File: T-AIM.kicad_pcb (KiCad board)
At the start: 2 copper layers, 3 parts, among them IC1 ATMEGA328PB-A, U1 V7805-500-SMT, U2 78L05

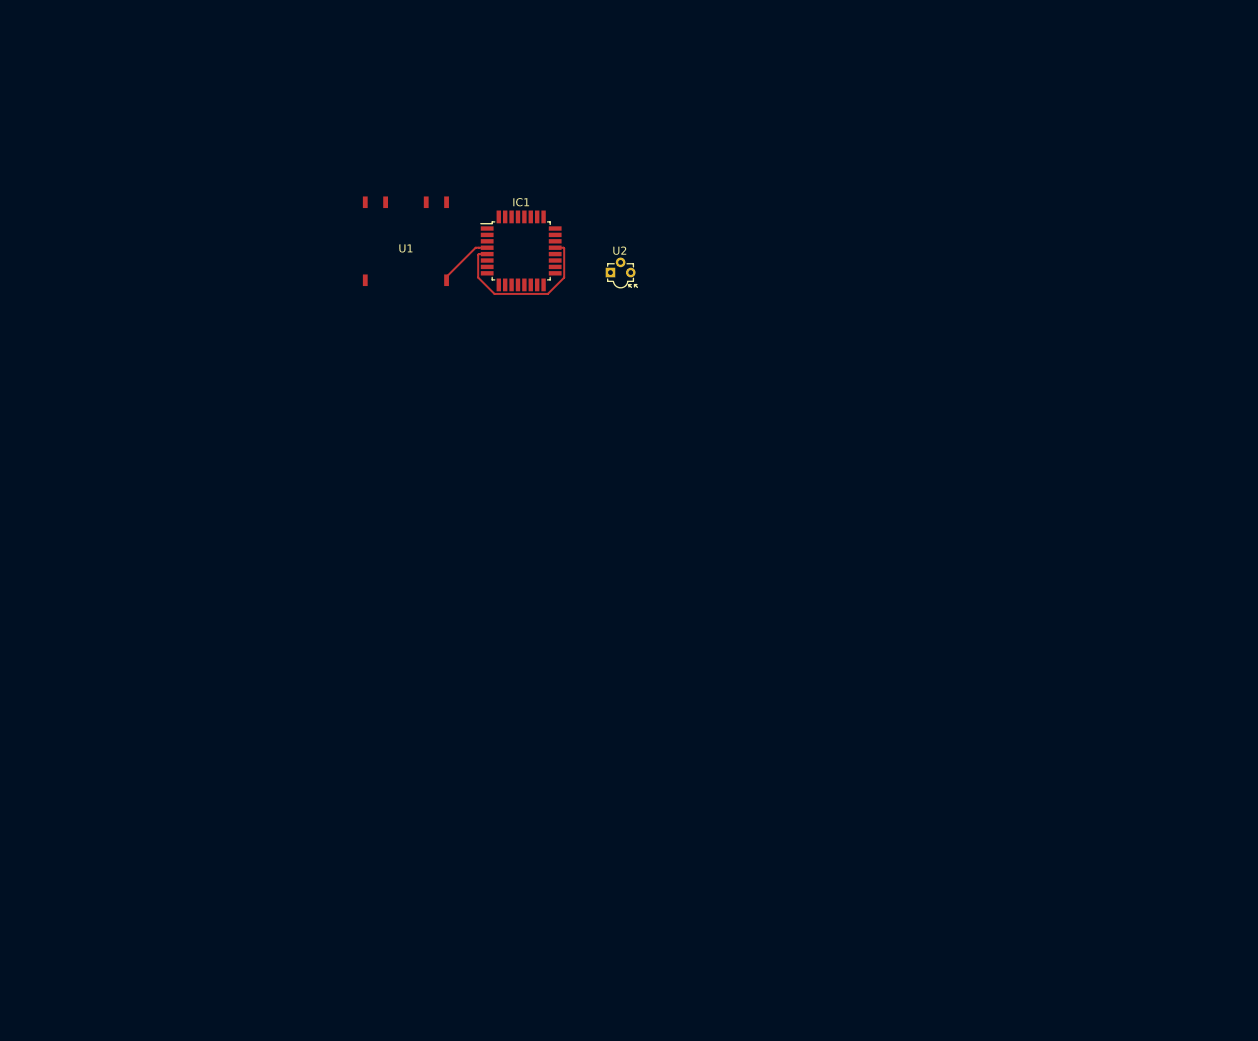
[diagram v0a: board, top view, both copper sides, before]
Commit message: Schematic switches changed; PCB footprints assigned; Preliminary PCB layout set
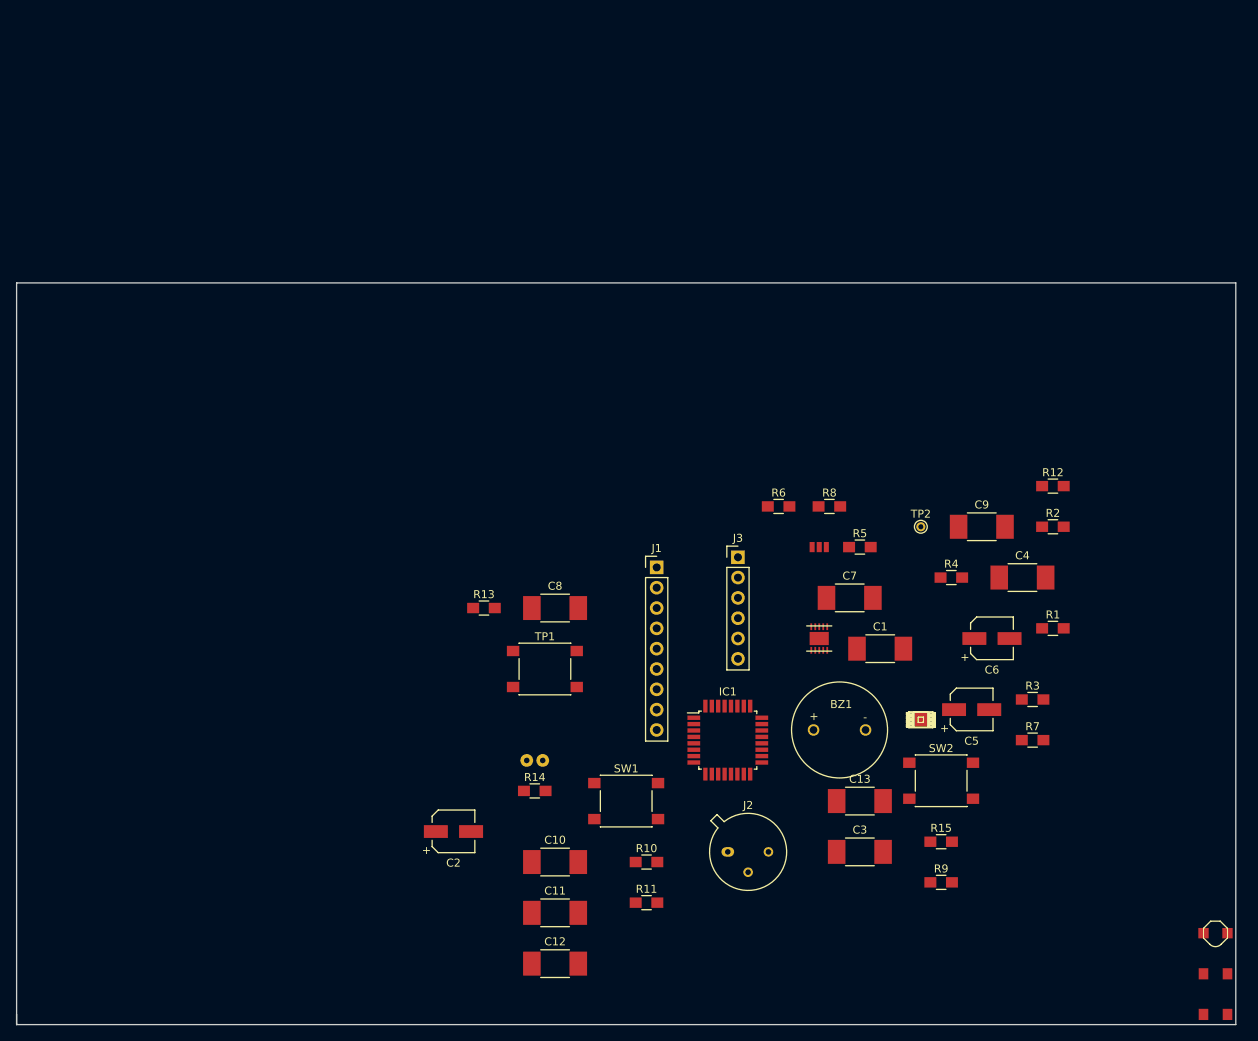
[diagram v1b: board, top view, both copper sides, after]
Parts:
- removed U2: 78L05, Opto-Devices:OPIC_Sharp_IS485
- added BZ1: Alarm Buzzer, T-AIM:AT-1220-TT-9-R, F.Cu at (167.6, 106.7)
- added C1: 10uF, Capacitors_SMD:C_1812_HandSoldering, F.Cu at (172.7, 96.5)
- added C10: 22uF, Capacitors_SMD:C_1812_HandSoldering, F.Cu at (132.1, 123.2)
- added C11: 0.1uF, Capacitors_SMD:C_1812_HandSoldering, F.Cu at (132.1, 129.5)
- added C12: 0.1uF, Capacitors_SMD:C_1812_HandSoldering, F.Cu at (132.1, 135.9)
- added C13: 0.1uF, Capacitors_SMD:C_1812_HandSoldering, F.Cu at (170.2, 115.6)
- added C2: 10uF, Capacitors_SMD:CP_Elec_5x5.3, F.Cu at (119.4, 119.4)
- added C3: 0.1uF, Capacitors_SMD:C_1812_HandSoldering, F.Cu at (170.2, 121.9)
- added C4: 0.1uF, Capacitors_SMD:C_1812_HandSoldering, F.Cu at (190.5, 87.6)
- added C5: 1uF, Capacitors_SMD:CP_Elec_5x5.3, F.Cu at (184.2, 104.1)
- added C6: 10nF, Capacitors_SMD:CP_Elec_5x5.3, F.Cu at (186.7, 95.2)
- added C7: 0.1uF, Capacitors_SMD:C_1812_HandSoldering, F.Cu at (168.9, 90.2)
- added C8: 22pF, Capacitors_SMD:C_1812_HandSoldering, F.Cu at (132.1, 91.4)
- added C9: 22pF, Capacitors_SMD:C_1812_HandSoldering, F.Cu at (185.4, 81.3)
- added D1: Red LED, SparkFun-LED:LED-1206, F.Cu at (214.6, 137.2)
- added D2: Blue LED, SparkFun-LED:LED-1206, F.Cu at (214.6, 142.2)
- added IC2: MAX17043, SparkFun-PowerIC:TDFN-8, F.Cu at (177.8, 105.4)
- added J1: ADXL345 Connector, Pin_Headers:Pin_Header_Straight_1x09_Pitch2.54mm, F.Cu at (144.8, 86.4)
- added J2: PIR Sensor Connector, TO_SOT_Packages_THT:TO-5-3, F.Cu at (153.7, 121.9)
- added J3: JY-MCU HC-05 Pins, Pin_Headers:Pin_Header_Straight_1x06_Pitch2.54mm, F.Cu at (154.9, 85.1)
- added JP1: M02JST-PTH-2, SparkFun-Connectors:JST-2-PTH, F.Cu at (129.5, 110.5)
- added L1: 4.7uH, 1.2A, SparkFun-Passives:INDUCTOR_4.7UH, F.Cu at (214.6, 132.1)
- added R1: 2M, Resistors_SMD:R_0805_HandSoldering, F.Cu at (194.3, 94.0)
- added R10: 10k, Resistors_SMD:R_0805_HandSoldering, F.Cu at (143.5, 123.2)
- added R11: 1k, Resistors_SMD:R_0805_HandSoldering, F.Cu at (143.5, 128.3)
- added R12: 220, Resistors_SMD:R_0805_HandSoldering, F.Cu at (194.3, 76.2)
- added R13: 220, Resistors_SMD:R_0805_HandSoldering, F.Cu at (123.2, 91.4)
- added R14: 10k, Resistors_SMD:R_0805_HandSoldering, F.Cu at (129.5, 114.3)
- added R15: 10k, Resistors_SMD:R_0805_HandSoldering, F.Cu at (180.3, 120.7)
- added R2: 220k, Resistors_SMD:R_0805_HandSoldering, F.Cu at (194.3, 81.3)
- added R3: 1k, Resistors_SMD:R_0805_HandSoldering, F.Cu at (191.8, 102.9)
- added R4: 150, Resistors_SMD:R_0805_HandSoldering, F.Cu at (181.6, 87.6)
- added R5: 220k, Resistors_SMD:R_0805_HandSoldering, F.Cu at (170.2, 83.8)
- added R6: 1.2M, Resistors_SMD:R_0805_HandSoldering, F.Cu at (160.0, 78.7)
- added R7: 4.7k, Resistors_SMD:R_0805_HandSoldering, F.Cu at (191.8, 108.0)
- added R8: 2M, Resistors_SMD:R_0805_HandSoldering, F.Cu at (166.4, 78.7)
- added R9: 10k, Resistors_SMD:R_0805_HandSoldering, F.Cu at (180.3, 125.7)
- added SJ1: SOLDERJUMPER_2WAY-OLDPASTE1&2, SparkFun-Passives:SJ_3, F.Cu at (165.1, 83.8)
- added SW1: Connection Button, Buttons_Switches_SMD:SW_SPST_PTS645, F.Cu at (141.0, 115.6)
- added SW2: Reset Button, Buttons_Switches_SMD:SW_SPST_PTS645, F.Cu at (180.3, 113.0)
- added TP1: ExtOsc, Buttons_Switches_SMD:SW_SPST_PTS645, F.Cu at (130.8, 99.1)
- added TP2: ExtOsc, Connectors:PINTST, F.Cu at (177.8, 81.3)
- U1: value V7805-500-SMT -> TPS61200; footprint T-AIM:V78-500-SMT -> SparkFun-PowerIC:DRC-10
- moved U1 74.6 mm to (165.1, 95.2)
- moved IC1 66.4 mm to (153.7, 108.0)
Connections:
- net Net-(IC1-Pad1) renamed RedLED
- net Net-(IC1-Pad2) renamed BlueLED
- IC1 pad 10: Net-(IC1-Pad10) -> FuelGaugeRestart
- IC1 pad 11: Net-(IC1-Pad11) -> BatteryLowAlert
- IC1 pad 12: Net-(IC1-Pad12) -> ConnectedButton
- IC1 pad 13: Net-(IC1-Pad13) -> PIR_OUT
- IC1 pad 18: Net-(IC1-Pad18) -> 3V3
- IC1 pad 27: Net-(IC1-Pad27) -> /SDA
- IC1 pad 28: Net-(IC1-Pad28) -> /SCL
- IC1 pad 29: Net-(IC1-Pad29) -> ResetButton
- IC1 pad 30: Net-(IC1-Pad30) -> BL_RXD
- IC1 pad 31: Net-(IC1-Pad31) -> BL_TXD
- IC1 pad 32: Net-(IC1-Pad32) -> INT1
- IC1 pad 4: VCC -> 3V3
- IC1 pad 6: Test1 -> Net-(IC1-Pad6)
- IC1 pad 9: Net-(IC1-Pad9) -> AlarmBuzzer
- U1 pad 10: Test1 -> Net-(R5-Pad1)
- U1 pad 6: Net-(U1-Pad6) -> VCC
- U1 pad 9: Net-(U1-Pad9) -> GND
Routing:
- net GND: track 21.3 -> 0.00 mm
- net VCC: track 7.01 -> 0.00 mm
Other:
- board outline added: 152.4 x 92.7 mm

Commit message: Layout started
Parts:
- D1, D2: footprint SparkFun-LED:LED-1206 -> LEDs:LED_1206
- L1: footprint SparkFun-Passives:INDUCTOR_4.7UH -> T-AIM:INDUCTOR_4.7UH
- TP1: footprint Buttons_Switches_SMD:SW_SPST_PTS645 -> Connectors:PINTST
- moved L1 118.1 mm to (129.5, 50.2), turned to 180 degrees
- moved C11 108.8 mm to (207.9, 51.5), turned to 270 degrees
- moved C12 107.3 mm to (198.4, 51.5), turned to 270 degrees
- moved C2 95.7 mm to (187.5, 52.1), turned to 180 degrees
- moved C4 94.3 mm to (96.6, 78.6), turned to 90 degrees
- moved D2 93.6 mm to (141.6, 83.6)
- moved R1 90.7 mm to (105.2, 77.0), turned to 90 degrees
- moved D1 83.5 mm to (147.6, 87.4)
- moved R11 75.7 mm to (191.7, 69.9)
- moved J1 73.9 mm to (179.0, 20.9)
- moved R14 73.5 mm to (199.5, 136.7), turned to 180 degrees
- moved R15 66.6 mm to (154.0, 59.5)
- moved C3 63.1 mm to (190.3, 62.1), turned to 270 degrees
- moved R2 62.5 mm to (132.6, 71.3), turned to 270 degrees
- moved C10 61.3 mm to (153.3, 65.7)
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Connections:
- IC1 pad 1: RedLED -> BlueLED
- IC1 pad 10: FuelGaugeRestart -> Net-(IC1-Pad10)
- IC1 pad 11: BatteryLowAlert -> Net-(IC1-Pad11)
- IC1 pad 12: ConnectedButton -> Net-(IC1-Pad12)
- IC1 pad 19: Net-(IC1-Pad19) -> ConnectedButton
- IC1 pad 2: BlueLED -> RedLED
- IC1 pad 24: Net-(IC1-Pad24) -> AlarmBuzzer
- IC1 pad 25: Net-(IC1-Pad25) -> FuelGaugeRestart
- IC1 pad 26: Net-(IC1-Pad26) -> BatteryLowAlert
- IC1 pad 9: AlarmBuzzer -> Net-(IC1-Pad9)

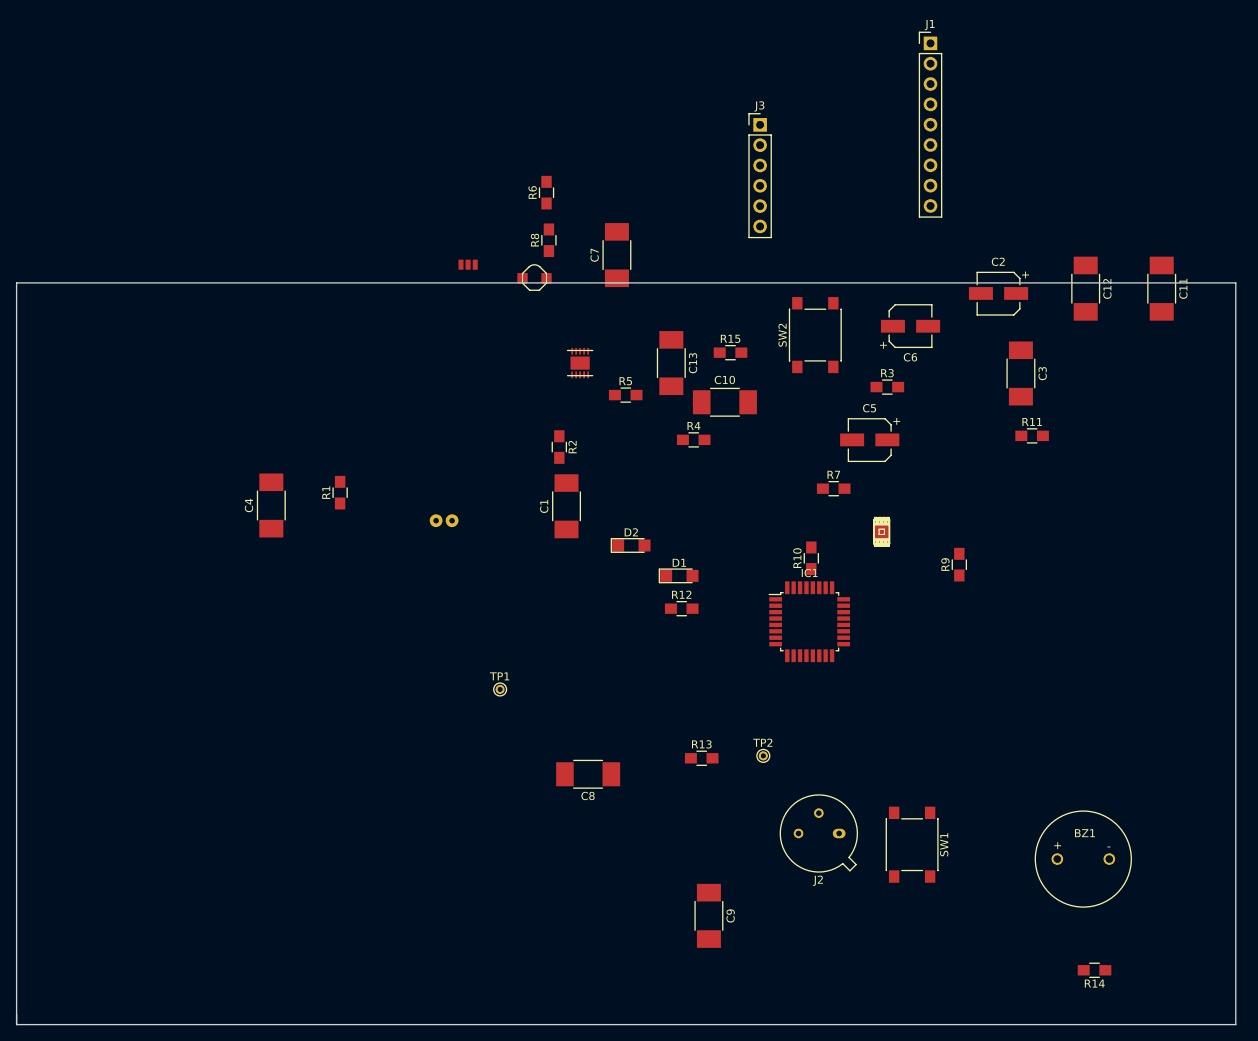
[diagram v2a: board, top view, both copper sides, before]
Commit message: Components placed to layout
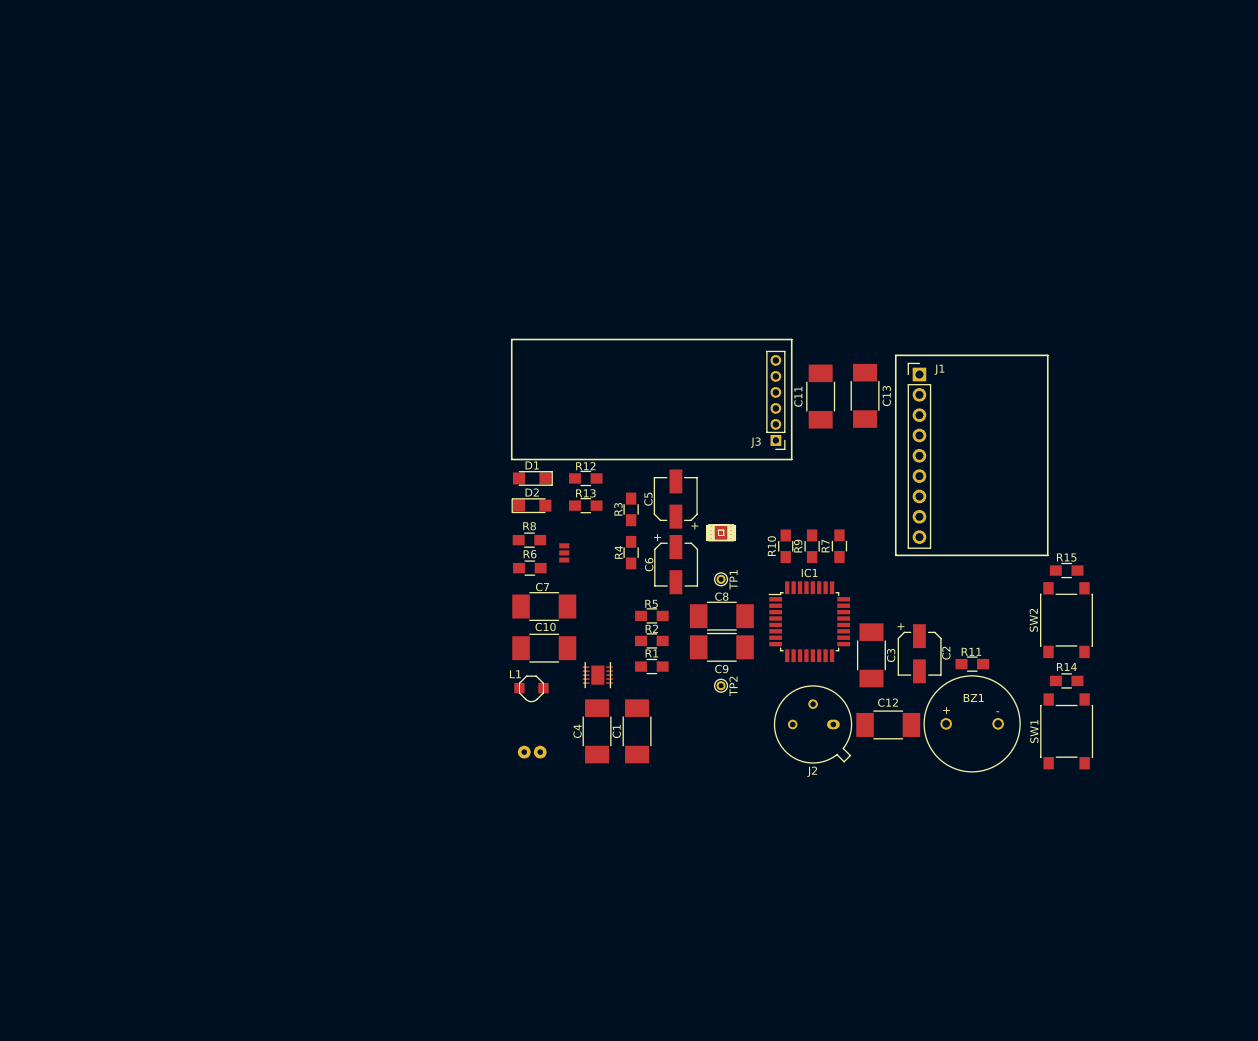
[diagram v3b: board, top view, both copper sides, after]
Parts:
- J3: footprint Pin_Headers:Pin_Header_Straight_1x06_Pitch2.54mm -> Pin_Headers:Pin_Header_Straight_1x06_Pitch2.00mm
- moved C12 59.9 mm to (173.7, 106.1), turned to 0 degrees
- moved L1 51.2 mm to (129.1, 101.5), turned to 0 degrees
- moved R15 50.1 mm to (196.0, 86.8), turned to 180 degrees
- moved C4 49.5 mm to (137.3, 106.9), turned to 270 degrees
- moved SW2 47.5 mm to (196.0, 93.0)
- moved R6 47.0 mm to (128.9, 86.5), turned to 0 degrees
- moved C2 46.1 mm to (177.6, 97.2), turned to 270 degrees
- moved C7 44.9 mm to (130.7, 91.3), turned to 180 degrees
- moved C11 44.7 mm to (165.3, 65.0), turned to 90 degrees
- moved R1 44.6 mm to (144.2, 98.8), turned to 180 degrees
- moved C6 41.8 mm to (147.2, 86.0), turned to 270 degrees
- moved J1 41.4 mm to (177.6, 62.3)
- moved C3 39.9 mm to (171.6, 97.4)
- moved J3 39.5 mm to (159.7, 70.5), turned to 180 degrees
- moved U1 39.1 mm to (137.4, 99.8), turned to 90 degrees
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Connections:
- IC1 pad 1: BlueLED -> BatteryLowAlert
- IC1 pad 17: Net-(IC1-Pad17) -> AlarmBuzzer
- IC1 pad 24: AlarmBuzzer -> Net-(IC1-Pad24)
- IC1 pad 25: FuelGaugeRestart -> INT1
- IC1 pad 26: BatteryLowAlert -> Net-(IC1-Pad26)
- IC1 pad 3: Net-(IC1-Pad3) -> BlueLED
- IC1 pad 32: INT1 -> FuelGaugeRestart
- JP1 pad 1: GND -> VCC
- JP1 pad 2: VCC -> GND
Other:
- board outline removed
- net class Default: clearance 0.2 -> 0.25
- net class Power added: clearance 0.2, trace_width 0.2, via_dia 0.8, via_drill 0.4
- net class Signal added: clearance 0.1, trace_width 0.1, via_dia 0.8, via_drill 0.4
- rule trace_clearance: 0.2 -> 0.25
- rule trace_min: 0.2 -> 0.01
